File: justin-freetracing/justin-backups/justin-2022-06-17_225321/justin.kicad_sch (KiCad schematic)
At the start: 114 parts, among them J1 Conn_01x08_MountingPin, J2 Conn_02x03_Odd_Even, J3 Conn_01x08_MountingPin, J5 Barrel_Jack_Switch_Pin3Ring, K1 SW_Push, K10 SW_Push, K11 SW_Push, K12 SW_Push, K13 SW_Push, K14 SW_Push, K15 SW_Push, K16 SW_Push, K17 SW_Push, K18 SW_Push, K19 SW_Push, K2 SW_Push, K20 SW_Push, K21 SW_Push, K22 SW_Push, K23 SW_Push, K24 SW_Push, K25 SW_Push, K26 SW_Push, K27 SW_Push, K28 SW_Push, K29 SW_Push, K3 SW_Push, K30 SW_Push, K31 SW_Push, K32 SW_Push, K33 SW_Push, K34 SW_Push, K35 SW_Push, K36 SW_Push, K37 SW_Push, K38 SW_Push, K39 SW_Push, K4 SW_Push, K40 SW_Push, K41 SW_Push, K42 SW_Push, K43 SW_Push, K44 SW_Push, K45 SW_Push, K46 SW_Push, K47 SW_Push, K48 SW_Push, K49 SW_Push, K5 SW_Push, K6 SW_Push, K7 SW_Push, K8 SW_Push, K9 SW_Push, U1 ATmega1284-P, Y1 20MHz

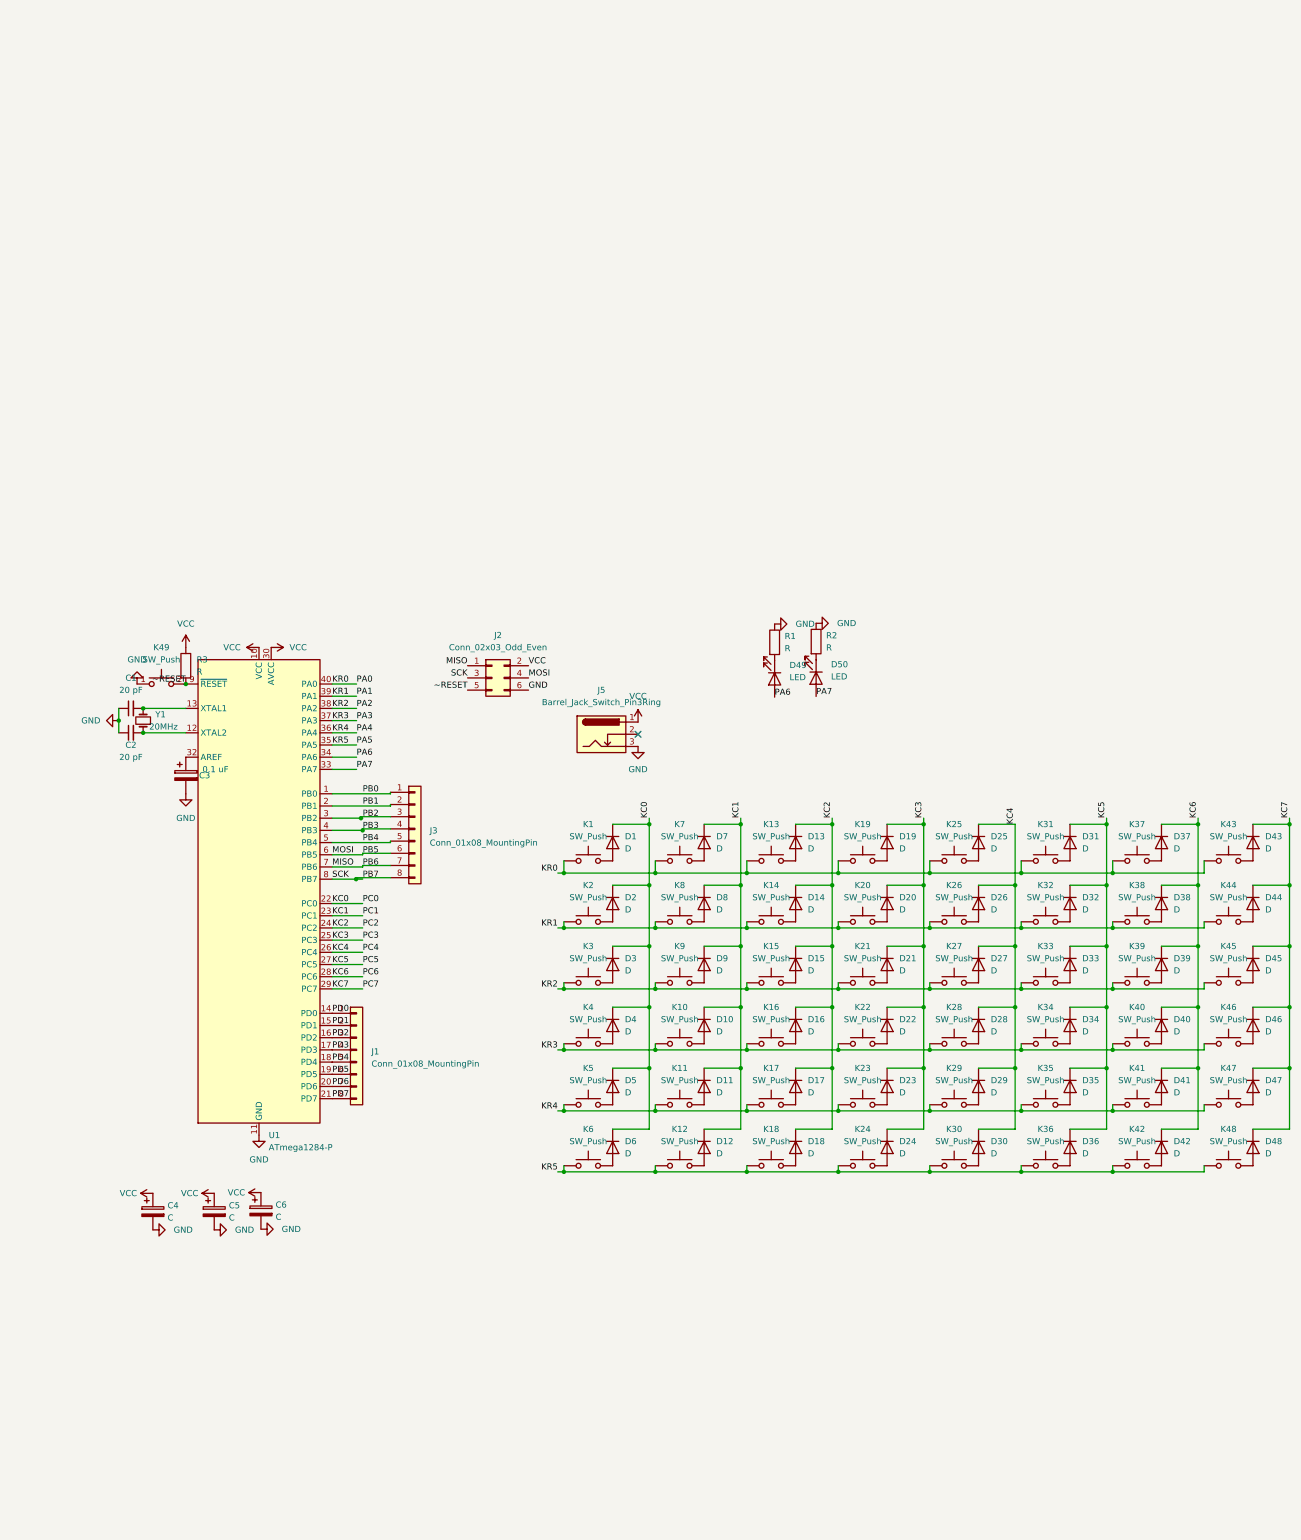
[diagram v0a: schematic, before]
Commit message: AVR Update
Clang Tidy
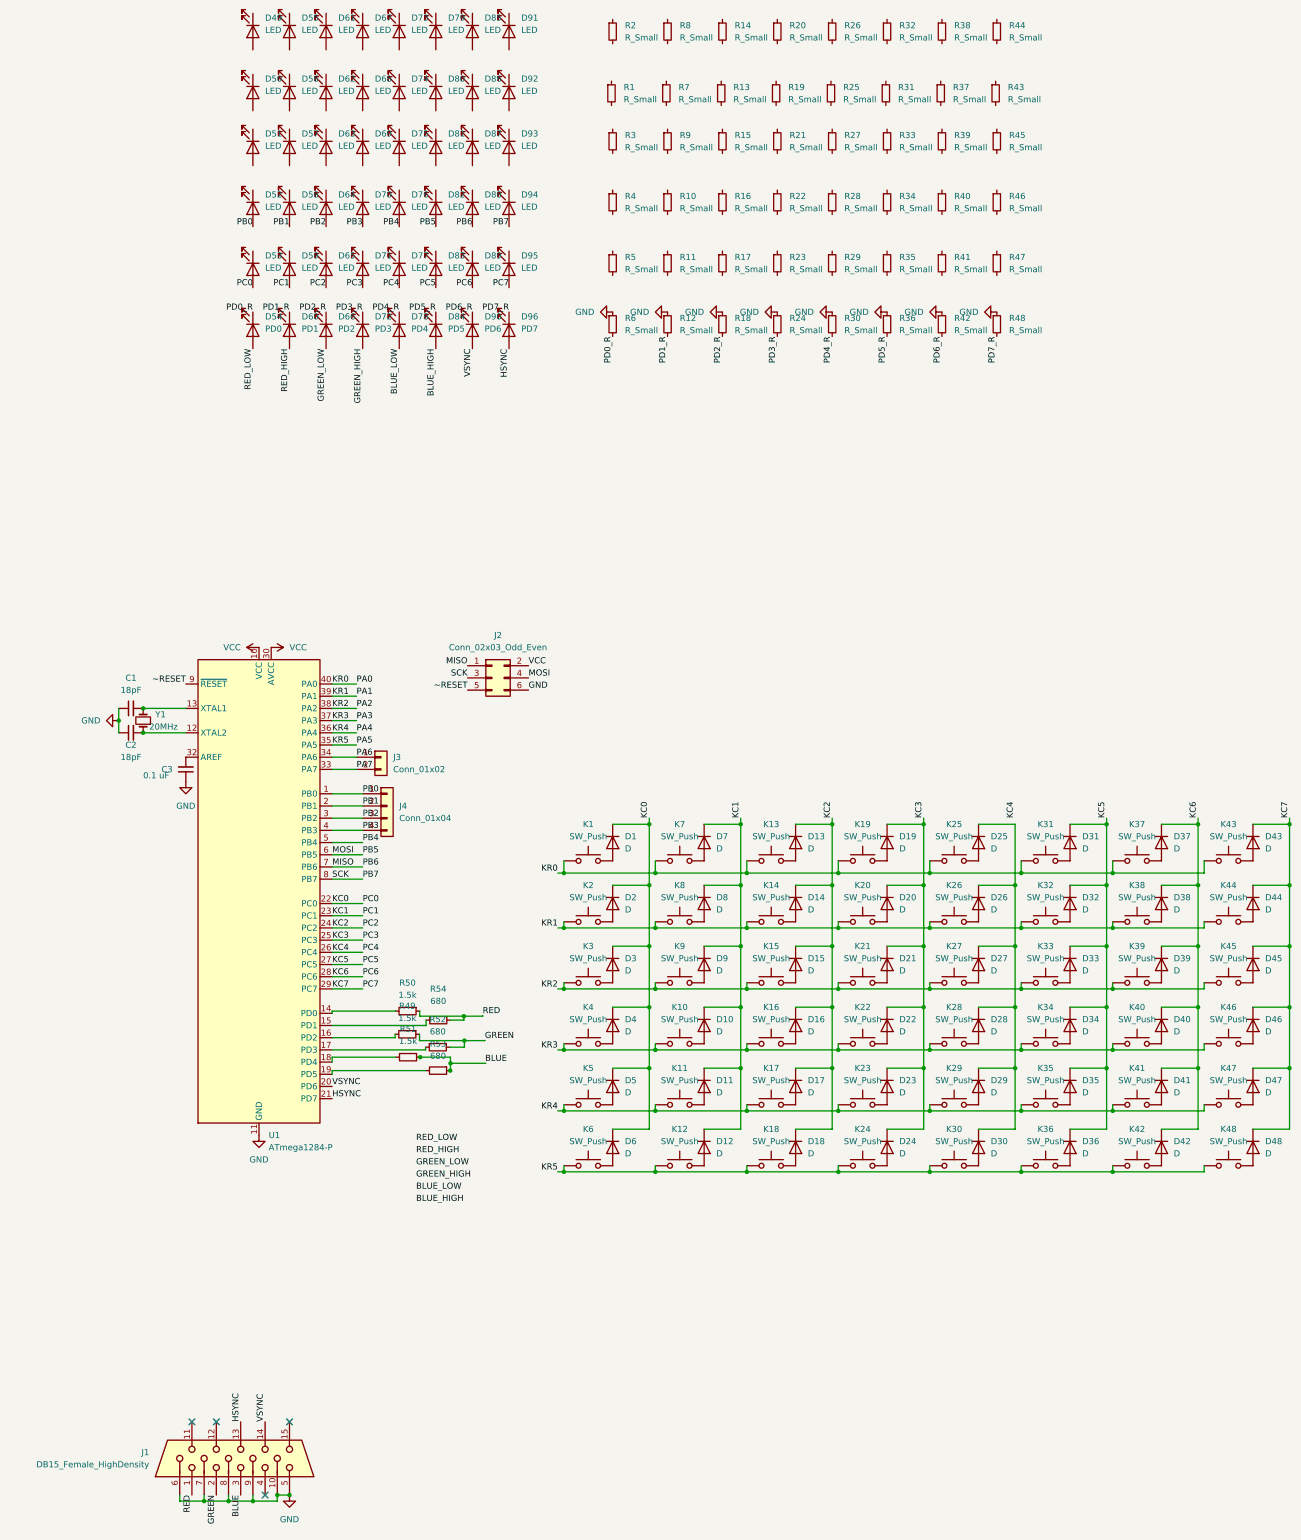
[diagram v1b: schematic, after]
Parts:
- removed C4, C5, C6: C, Capacitor_THT:CP_Radial_D5.0mm_P2.00mm, symbol Device:C_Polarized
- removed J1, J3: Conn_01x08_MountingPin, Connector_PinHeader_2.54mm:PinHeader_1x08_P2.54mm_Vertical, symbol Connector_Generic:Conn_01x08
- removed J5: Barrel_Jack_Switch_Pin3Ring, Connector_BarrelJack:BarrelJack_Horizontal, symbol Connector:Barrel_Jack_Switch_Pin3Ring
- removed K49: SW_Push, Button_Switch_Keyboard:SW_Cherry_MX_1.00u_PCB, symbol Switch:SW_Push
- removed R1, R2, R3: R, Resistor_THT:R_Axial_DIN0204_L3.6mm_D1.6mm_P5.08mm_Horizontal, symbol Device:R
- added D51, D52, D53, D55, D56, D57, D58, D59, D61, D62, D63, D64, D65, D67, D68, D69, D70, D71, D73, D74, D75, D76, D77, D79, D80, D81, D82, D83, D85, D86, D87, D88, D89, D91, D92, D93, D94, D95: LED, symbol Device:LED
- added D54: PD0, symbol Device:LED
- added D60: PD1, symbol Device:LED
- added D66: PD2, symbol Device:LED
- added D72: PD3, symbol Device:LED
- added D78: PD4, symbol Device:LED
- added D84: PD5, symbol Device:LED
- added D90: PD6, symbol Device:LED
- added D96: PD7, symbol Device:LED
- added J1: DB15_Female_HighDensity, Connector_Dsub:DSUB-15_Female_EdgeMount_P2.77mm, symbol Connector:DB15_Female_HighDensity
- added J3: Conn_01x02, Connector_PinHeader_2.00mm:PinHeader_1x02_P2.00mm_Vertical, symbol Connector_Generic:Conn_01x02
- added J4: Conn_01x04, Connector_PinHeader_2.00mm:PinHeader_1x04_P2.00mm_Vertical, symbol Connector_Generic:Conn_01x04
- added R1, R10, R11, R12, R13, R14, R15, R16, R17, R18, R19, R2, R20, R21, R22, R23, R24, R25, R26, R27, R28, R29, R3, R30, R31, R32, R33, R34, R35, R36, R37, R38, R39, R4, R40, R41, R42, R43, R44, R45, R46, R47, R48, R5, R6, R7, R8, R9: R_Small, symbol Device:R_Small
- added R49, R50, R51: 1.5k, Resistor_THT:R_Axial_DIN0204_L3.6mm_D1.6mm_P5.08mm_Horizontal, symbol Device:R_Small
- added R52, R53, R54: 680, Resistor_THT:R_Axial_DIN0204_L3.6mm_D1.6mm_P5.08mm_Horizontal, symbol Device:R_Small
- C1, C2: value 20 pF -> 18pF; footprint Capacitor_THT:C_Disc_D3.0mm_W1.6mm_P2.50mm -> Capacitor_THT:C_Axial_L3.8mm_D2.6mm_P7.50mm_Horizontal
- C3: footprint Capacitor_THT:CP_Radial_D5.0mm_P2.00mm -> Capacitor_THT:C_Axial_L3.8mm_D2.6mm_P7.50mm_Horizontal; symbol Device:C_Polarized -> Device:C_Small
- D49, D50: footprint LED_THT:LED_D5.0mm_Clear -> (none)
- J2: footprint Connector_PinHeader_2.54mm:PinHeader_2x03_P2.54mm_Vertical -> Connector_PinHeader_2.00mm:PinHeader_2x03_P2.00mm_Vertical
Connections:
- net GND: now also C3.1, J1.10, J1.5, J1.6, J1.7, J1.8, J1.9, R12.1, R18.1, R24.1, R30.1, R36.1, R42.1, R48.1, R6.1; no longer C3.2
- net KC0: now also D53.2 (A)
- net KC1: now also D59.2 (A)
- net KC2: now also D65.2 (A)
- net KC3: now also D71.2 (A)
- net KC4: now also D77.2 (A); no longer D25.1 (K), D26.1 (K), D27.1 (K), D28.1 (K), D29.1 (K), D30.1 (K)
- net KC5: now also D83.2 (A)
- net KC6: now also D89.2 (A)
- net KC7: now also D95.2 (A)
- net MISO: now also D88.2 (A)
- net MOSI: now also D82.2 (A)
- net PA6: now also J3.1 (Pin_1); no longer D49.2 (A)
- net PA7: now also J3.2 (Pin_2); no longer D50.2 (A)
- net PB0: now also D52.2 (A), J4.1 (Pin_1)
- net PB1: now also D58.2 (A), J4.2 (Pin_2)
- net PB2: now also D64.2 (A), J4.3 (Pin_3)
- net PB3: now also D70.2 (A), J4.4 (Pin_4)
- net PB4: now also D76.2 (A)
- net PB7: now also D94.2 (A)
- net at U1.32 (AREF): now also C3.2; no longer C3.1
- net PD0: no longer names the net of U1.14 (PD0)
- net PD0: now also R50.2
- net PD1: no longer names the net of U1.15 (PD1)
- net PD1: now also R54.2
- net PD2: no longer names the net of U1.16 (PD2)
- net PD2: now also R49.2
- net PD3: no longer names the net of U1.17 (PD3)
- net PD3: now also R52.2
- net PD4: no longer names the net of U1.18 (PD4)
- net PD4: now also R51.2
- net PD5: no longer names the net of U1.19 (PD5)
- net PD5: now also R53.2
- net PD6 renamed VSYNC
- net VSYNC: now also D90.2 (A), J1.14
- net PD7 renamed HSYNC
- net HSYNC: now also D96.2 (A), J1.13
- new net: D25.1 (K), D26.1 (K), D27.1 (K), D28.1 (K), D29.1 (K), D30.1 (K)
- new net BLUE: J1.3, R51.1, R53.1
- new net BLUE_HIGH: D84.2 (A)
- new net BLUE_LOW: D78.2 (A)
- new net GREEN: J1.2, R49.1, R52.1
- new net GREEN_HIGH: D72.2 (A)
- new net GREEN_LOW: D66.2 (A)
- new net PD0_R: D54.1 (K), R6.2
- new net PD1_R: D60.1 (K), R12.2
- new net PD2_R: D66.1 (K), R18.2
- new net PD3_R: D72.1 (K), R24.2
- new net PD4_R: D78.1 (K), R30.2
- new net PD5_R: D84.1 (K), R36.2
- new net PD6_R: D90.1 (K), R42.2
- new net PD7_R: D96.1 (K), R48.2
- new net RED: J1.1, R50.1, R54.1
- new net RED_HIGH: D60.2 (A)
- new net RED_LOW: D54.2 (A)
- no-connect marks 1 -> 4
